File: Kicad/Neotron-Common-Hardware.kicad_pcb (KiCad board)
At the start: 4 copper layers, 243.8 x 243.8 mm, 256 parts, among them J1001 USB Ports External, J1002 USB Ports Internal, J101 Neotron-Expansion-Slot, J102 Neotron-Expansion-Slot, J103 Neotron-Expansion-Slot, J104 Neotron-Expansion-Slot, J1101 RJ45 MagJack, J201 DE15HD, J601 Line Out, J602 AC'97 Audio Header, J603 CD Audio In, J701 SD_Card, J801 Conn_02x05, J802 DB9_Male_MountingHoles, J901 Jack-DC, J902 Double-mini-DIN-6, Q901 BC548, SW901 SW_DIP_x01, SW902 SW_DIP_x01, U1001 AP2501, U1002 MIC2005A-2YM5, U1003 MIC2005A-2YM5, U1004 XR22404CG28, U1005 MIC2005A-2YM5, U1006 MIC2005A-2YM5, U101 Neotron-CPU, U1101 ENC424J600, U1201 MCP7940, U201 THS7316, U202 TPD7S019, U601 TLV320AIC23BPW, U602 STX-4335-5BGP-S1, U801 ST3232CDR, U901 5V DC-DC Module, U902 TLV1117 3.3V 1A, U903 MAX1615, U904 STM32F030F4Px, Y1001 12M, Y1101 25M, Y1201 32,768 Hz, Y601 12M

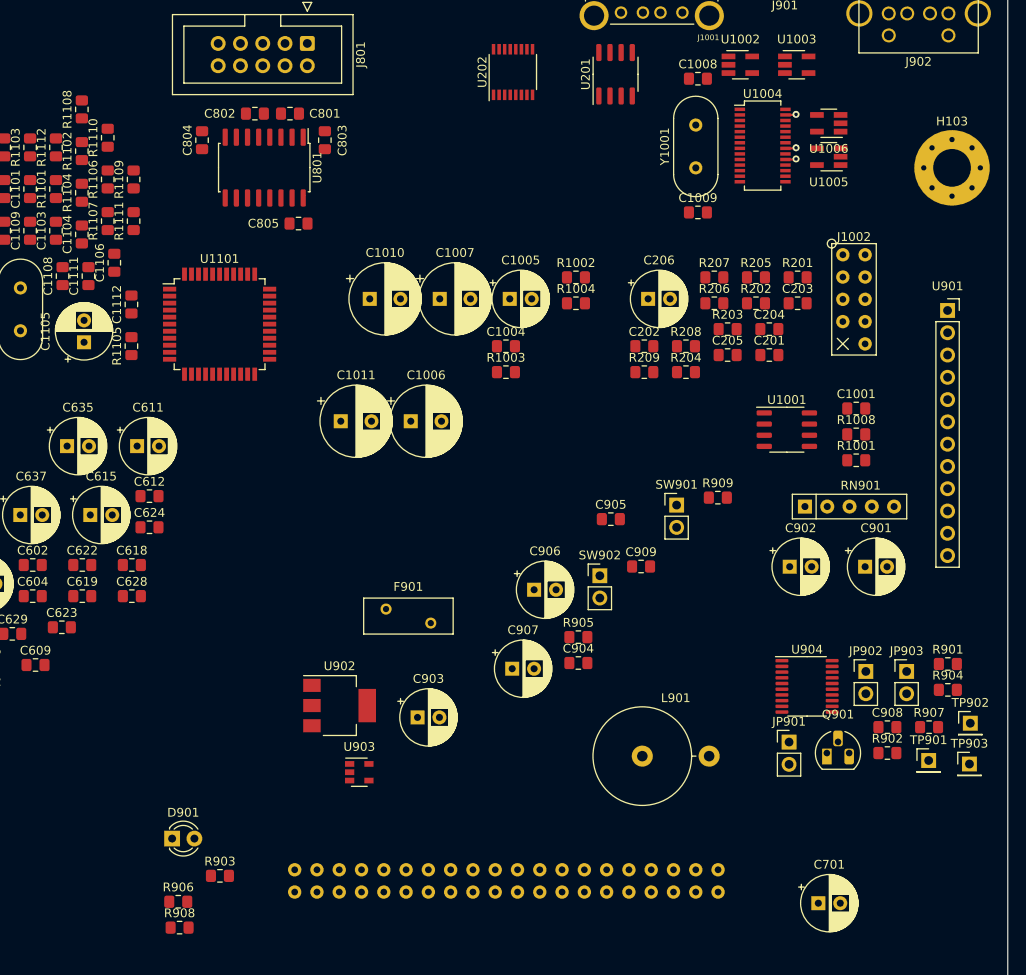
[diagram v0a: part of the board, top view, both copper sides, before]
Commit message: Updated PCB from Schematic.
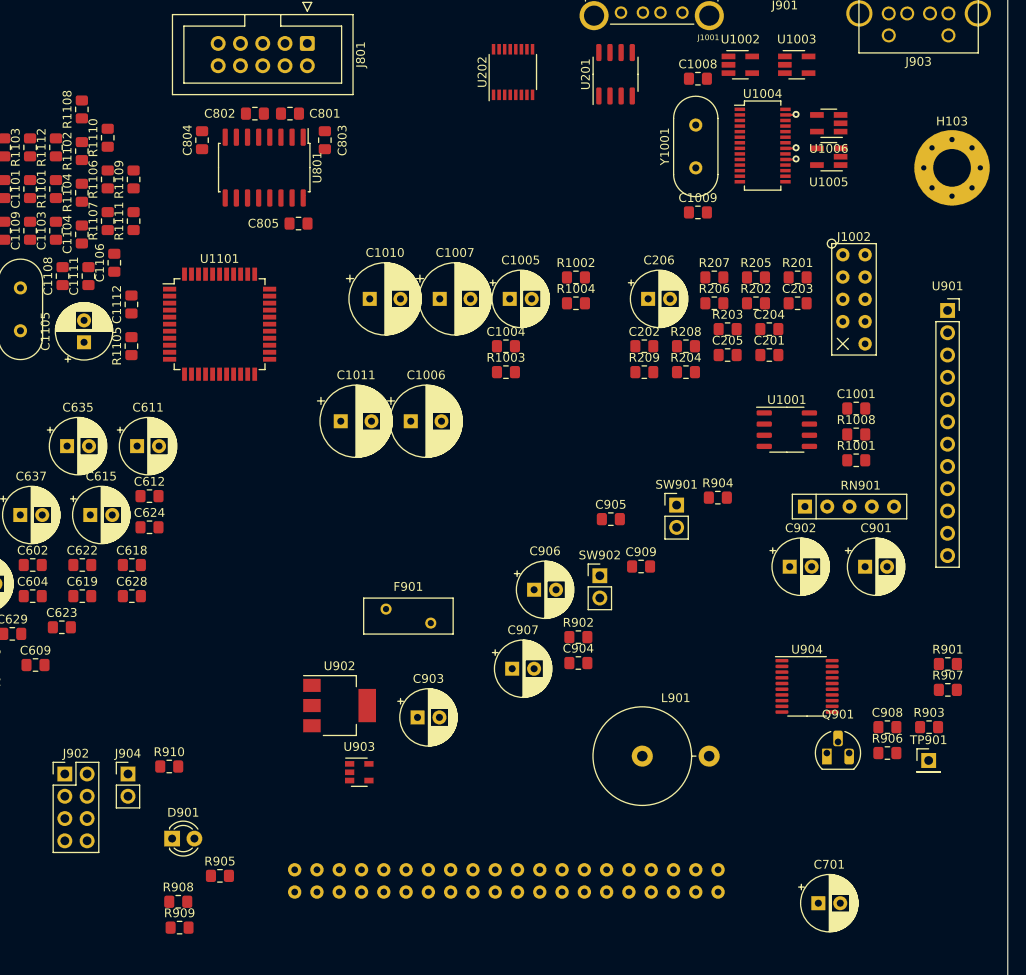
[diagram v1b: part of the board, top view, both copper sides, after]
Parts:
- removed JP901, JP902, JP903: Jumper, Connector_PinHeader_2.54mm:PinHeader_1x02_P2.54mm_Vertical
- removed TP902, TP903: TestPoint, Connector_PinHeader_2.54mm:PinHeader_1x01_P2.54mm_Vertical
- added J902: Conn_02x04_Odd_Even, Connector_PinHeader_2.54mm:PinHeader_2x04_P2.54mm_Vertical, F.Cu at (170.1, 133.3)
- added J904: Header, Connector_PinHeader_2.54mm:PinHeader_1x02_P2.54mm_Vertical, F.Cu at (177.3, 133.3)
- added R910: 1k, Resistor_SMD:R_0805_2012Metric_Pad1.15x1.40mm_HandSolder, F.Cu at (182.0, 132.4)
- renumbered J902 to J903, R905 to R902, R907 to R903, R909 to R904, R903 to R905, R902 to R906, R904 to R907, R906 to R908, R908 to R909
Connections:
- U901 pad 10: +5V -> (no net)
- U901 pad 11: +5V -> (no net)
- U901 pad 3: Net-(C902-Pad1) -> GND
- U901 pad 4: Net-(C902-Pad1) -> +5V
- U901 pad 5: GND -> (no net)
- U901 pad 6: GND -> (no net)
- U901 pad 7: GND -> (no net)
- U901 pad 8: GND -> (no net)
- U901 pad 9: +5V -> (no net)

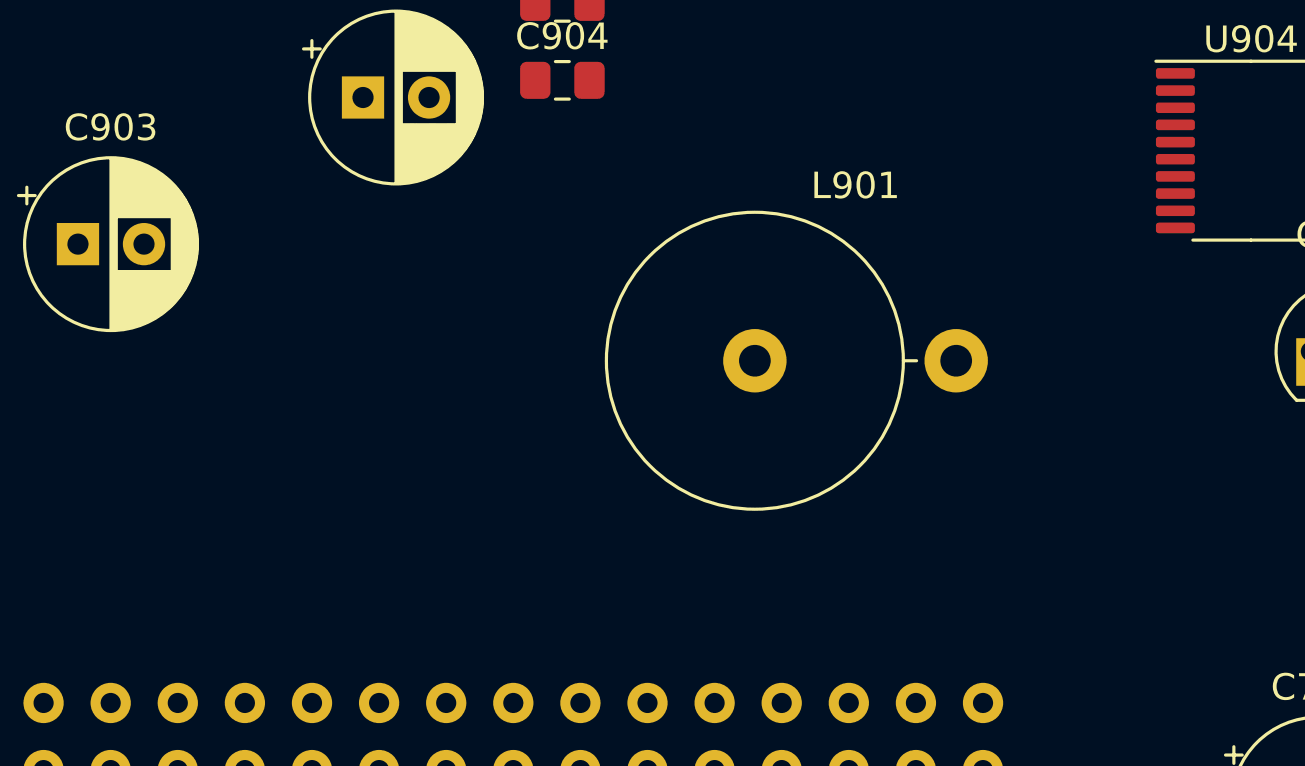
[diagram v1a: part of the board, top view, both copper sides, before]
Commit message: Replace inductor with horizontal footprint.
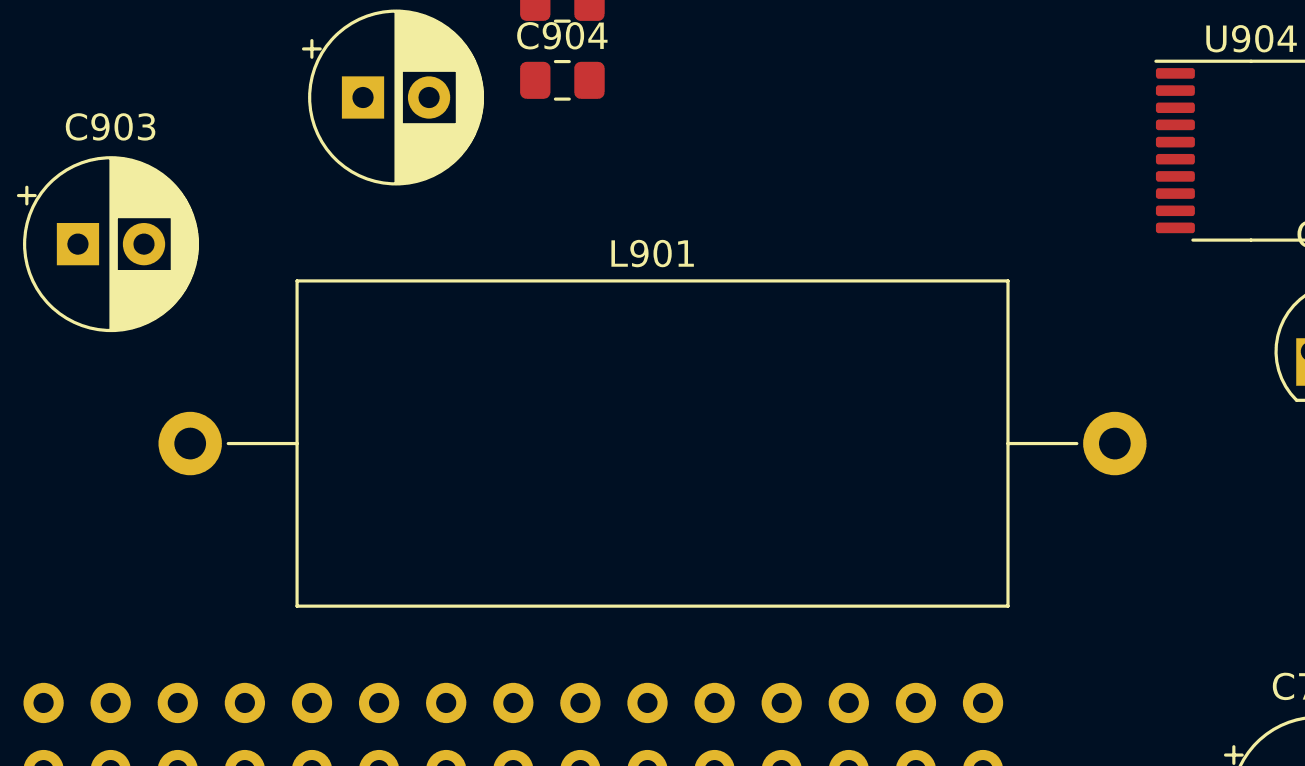
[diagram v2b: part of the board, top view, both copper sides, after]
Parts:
- L901: footprint Inductor_THT:L_Axial_L26.0mm_D11.0mm_P7.62mm_Vertical_Fastron_77A -> Inductor_THT:L_Axial_L26.7mm_D12.1mm_P35.00mm_Horizontal_Vishay_IHA-103
- moved L901 21.6 mm to (214.6, 134.4)

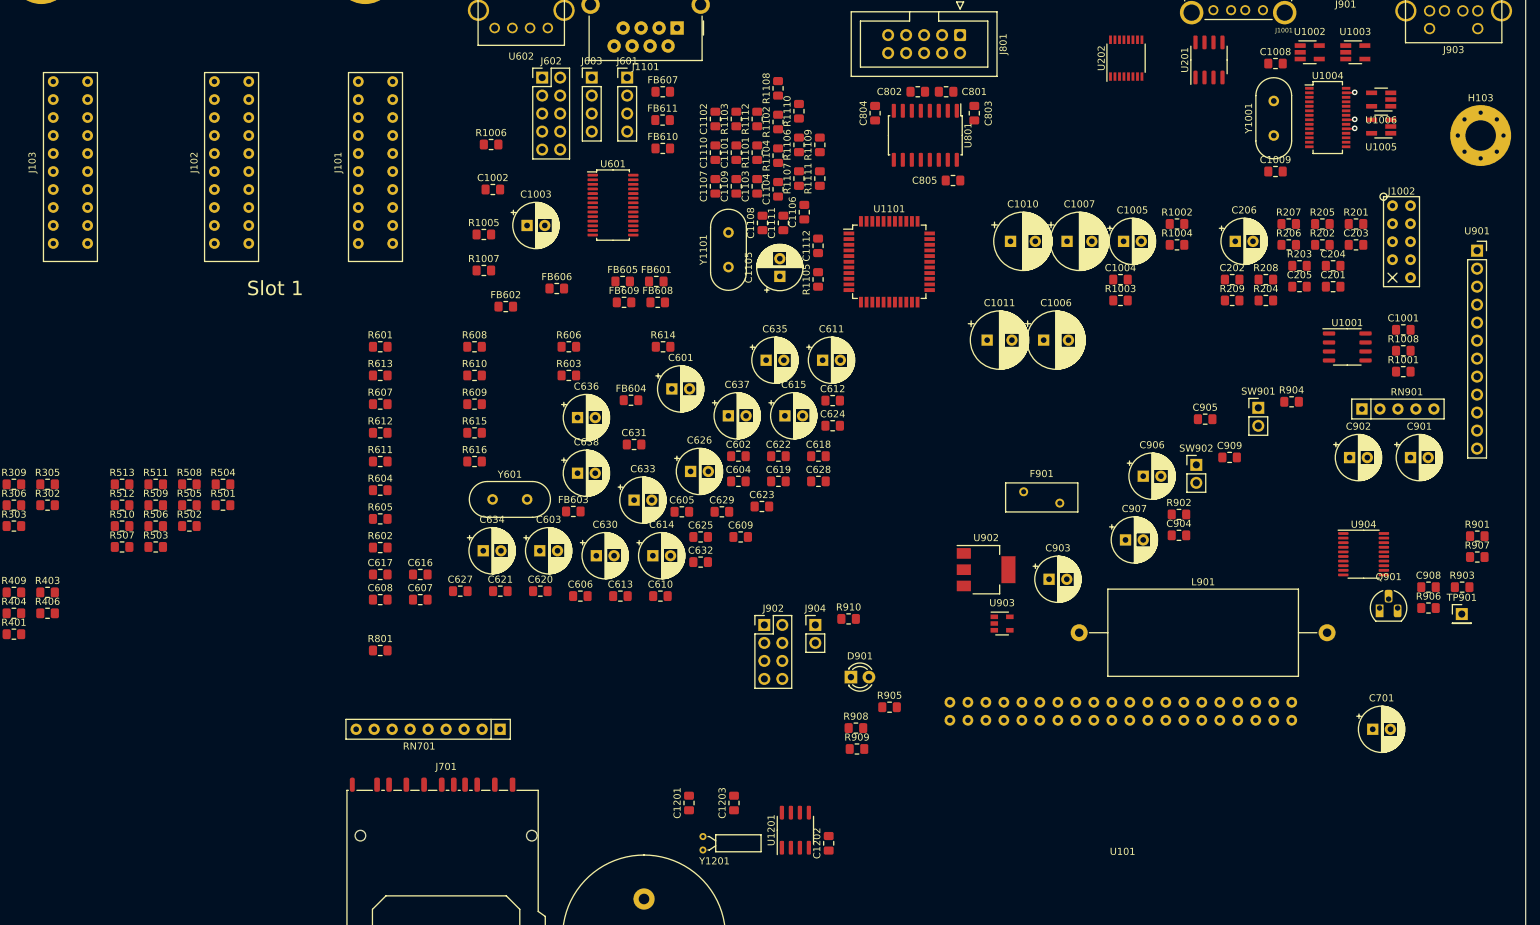
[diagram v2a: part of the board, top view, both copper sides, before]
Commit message: Switch some of the radial THT Electrolytic caps for SMD MLCCs.
Also changed the STM32 for an LQFP-32 as it has a bigger pitch on the
pins.

The LQFP is easier to solder than the TSSOP, and the MLCC takes are
cheaper and take up less space.
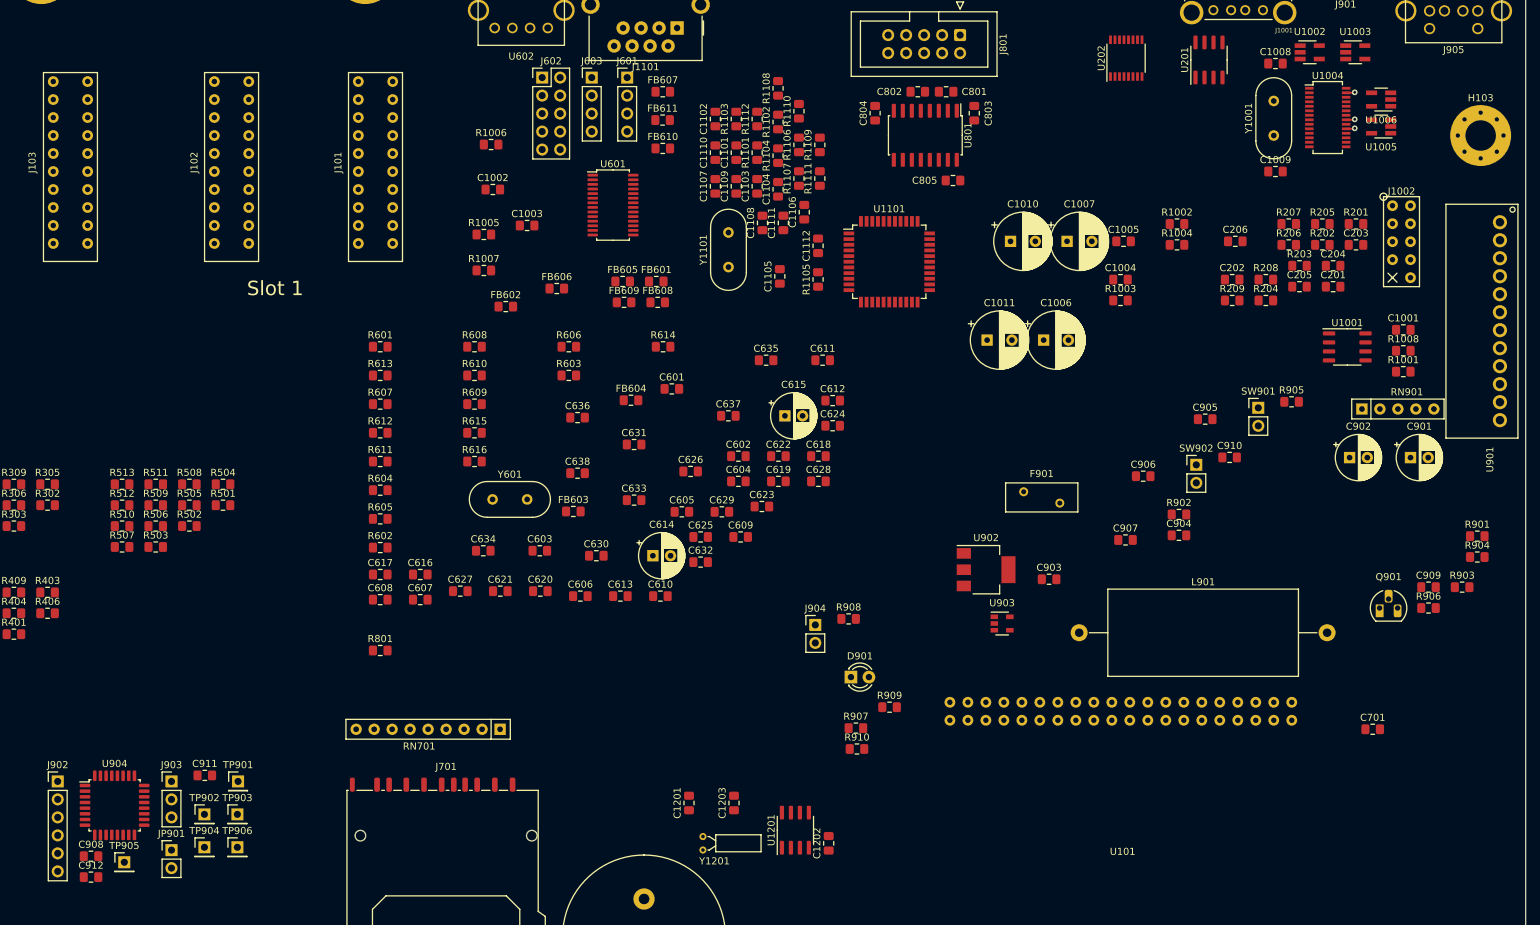
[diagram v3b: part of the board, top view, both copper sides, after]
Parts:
- added C908: 100n, Capacitor_SMD:C_0805_2012Metric_Pad1.15x1.40mm_HandSolder, F.Cu at (75.1, 165.9)
- added C911: 10n, Capacitor_SMD:C_0805_2012Metric_Pad1.15x1.40mm_HandSolder, F.Cu at (91.1, 154.5)
- added C912: 1u 10V, Capacitor_SMD:C_0805_2012Metric_Pad1.15x1.40mm_HandSolder, F.Cu at (75.1, 168.9)
- added J903: Conn_01x03, Connector_PinHeader_2.54mm:PinHeader_1x03_P2.54mm_Vertical, F.Cu at (86.4, 155.4)
- added JP901: Jumper, Connector_PinHeader_2.54mm:PinHeader_1x02_P2.54mm_Vertical, F.Cu at (86.4, 165.1)
- added TP902: TestPoint_Small, Connector_PinHeader_2.54mm:PinHeader_1x01_P2.54mm_Vertical, F.Cu at (91.1, 160.0)
- added TP903: TestPoint_Small, Connector_PinHeader_2.54mm:PinHeader_1x01_P2.54mm_Vertical, F.Cu at (95.7, 160.0)
- added TP904: TestPoint_Small, Connector_PinHeader_2.54mm:PinHeader_1x01_P2.54mm_Vertical, F.Cu at (91.1, 164.7)
- added TP905: TestPoint_Small, Connector_PinHeader_2.54mm:PinHeader_1x01_P2.54mm_Vertical, F.Cu at (79.8, 166.8)
- added TP906: TestPoint_Small, Connector_PinHeader_2.54mm:PinHeader_1x01_P2.54mm_Vertical, F.Cu at (95.7, 164.7)
- BT1201: value Coin Cell -> CR2032
- C1003, C1005, C907: value 4u7 -> 4u7 10V; footprint Capacitor_THT:CP_Radial_D6.3mm_P2.50mm -> Capacitor_SMD:C_0805_2012Metric_Pad1.15x1.40mm_HandSolder
- C1006, C1007, C1010, C1011: value 120u -> 120u 16V
- C1105, C906: footprint Capacitor_THT:CP_Radial_D6.3mm_P2.50mm -> Capacitor_SMD:C_0805_2012Metric_Pad1.15x1.40mm_HandSolder
- C206, C601, C603, C611, C626, C633, C634, C635, C636, C637, C638, C701: value 10u -> 10u 10V; footprint Capacitor_THT:CP_Radial_D6.3mm_P2.50mm -> Capacitor_SMD:C_0805_2012Metric_Pad1.15x1.40mm_HandSolder
- C614, C615: value 220u -> 220u 16V
- C630: value 1u -> 1u 10V; footprint Capacitor_THT:CP_Radial_D6.3mm_P2.50mm -> Capacitor_SMD:C_0805_2012Metric_Pad1.15x1.40mm_HandSolder
- C903: value 22u -> 22u 16V; footprint Capacitor_THT:CP_Radial_D6.3mm_P2.50mm -> Capacitor_SMD:C_0805_2012Metric_Pad1.15x1.40mm_HandSolder
- C905: value 1u -> 1u 10V
- C910: renamed from C909; value 100n -> 4u7 10V
- FB601, FB602, FB603, FB604, FB605, FB606, FB608, FB609, FB610, FB611: value 220R@100MHz -> 3k3
- J902: value Conn_02x04_Odd_Even -> Conn_01x06; footprint Connector_PinHeader_2.54mm:PinHeader_2x04_P2.54mm_Vertical -> Connector_PinHeader_2.54mm:PinHeader_1x06_P2.54mm_Vertical
- R1102, R1106: value 10 -> 10R
- R1108, R1109: value 180 -> 180R
- R201, R202, R203: value 75 -> 75R
- R601, R602: value 100 -> 100R
- TP901: value TestPoint -> TestPoint_Small
- U901: footprint Connector_PinSocket_2.54mm:PinSocket_1x12_P2.54mm_Vertical -> Neotron-Common-Hardware:K78xx-3AR3
- U904: value STM32F030F4Px -> STM32F031K6T6; footprint Package_SO:TSSOP-20_4.4x6.5mm_P0.65mm -> Package_QFP:LQFP-32_7x7mm_P0.8mm
- moved U904 179.9 mm to (78.4, 158.8)
- moved TP901 174.4 mm to (95.8, 155.4)
- moved J902 102.2 mm to (70.4, 155.4)
- moved U901 9.26 mm to (274.0, 89.1), turned to 270 degrees
- renumbered C908 to C909, J903 to J905, R907 to R904, R904 to R905, R908 to R907, R910 to R908, R905 to R909, R909 to R910
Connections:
- C206 pad 1: GND -> +3V3
- C206 pad 2: +3V3 -> GND
- J902 pad 1: (no net) -> GND
- J902 pad 2: /Power Supply/SCL_U1TX -> /Power Supply/BOOT_RX
- J902 pad 3: (no net) -> /Power Supply/SWCLK_BOOT_TX
- J902 pad 4: /Power Supply/SDA_U1RX -> /Power Supply/SWDIO
- J902 pad 5: +3.3VP -> /Power Supply/~BMC_RST
- J902 pad 6: /Power Supply/~BMC_RST -> +3.3VP
- R904 pad 1: /Power Supply/BOOT0 -> Net-(JP901-Pad2)
- TP901 pad 1: /Power Supply/USART1_TX -> Net-(TP901-Pad1)
- U904 pad 1: /Power Supply/BOOT0 -> +3.3VP
- U904 pad 10: /Power Supply/DC_ON -> /Power Supply/~BUTTON_PWR
- U904 pad 11: (no net) -> /Power Supply/~STATUS_LED
- U904 pad 13: /Power Supply/~BUTTON_PWR -> Net-(TP903-Pad1)
- U904 pad 14: (no net) -> Net-(TP904-Pad1)
- U904 pad 15: GND -> Net-(TP905-Pad1)
- U904 pad 16: +3.3VP -> GND
- U904 pad 17: /Power Supply/SCL_U1TX -> +3.3VP
- U904 pad 18: /Power Supply/SDA_U1RX -> (no net)
- U904 pad 19: /Power Supply/PS2_DAT1 -> /Power Supply/PS2_DAT0
- U904 pad 2: /Power Supply/PS2_DAT0 -> Net-(TP901-Pad1)
- U904 pad 20: /Power Supply/PS2_CLK1 -> /Power Supply/PS2_CLK0
- U904 pad 3: /Power Supply/PS2_CLK0 -> Net-(TP902-Pad1)
- U904 pad 8: /Power Supply/USART1_TX -> /Power Supply/UART_TX
- U904 pad 9: /Power Supply/~STATUS_LED -> /Power Supply/UART_RX
